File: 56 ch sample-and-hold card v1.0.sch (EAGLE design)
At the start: 116 parts, among them IC1 4051D, IC10 TL074JT, IC11 4051D, IC12 TL074JT, IC13 TL074JT, IC14 4051D, IC15 TL074JT, IC16 TL074JT, IC17 4051D, IC18 TL074JT, IC19 TL074JT, IC20 4051D, IC21 TL074JT, IC22 TL074JT, IC26 4051D, IC27 TL074JT, IC28 TL074JT, IC3 TL074JT, IC5 78L05F, IC6 TL074JT, IC7 4051D, IC9 TL074JT

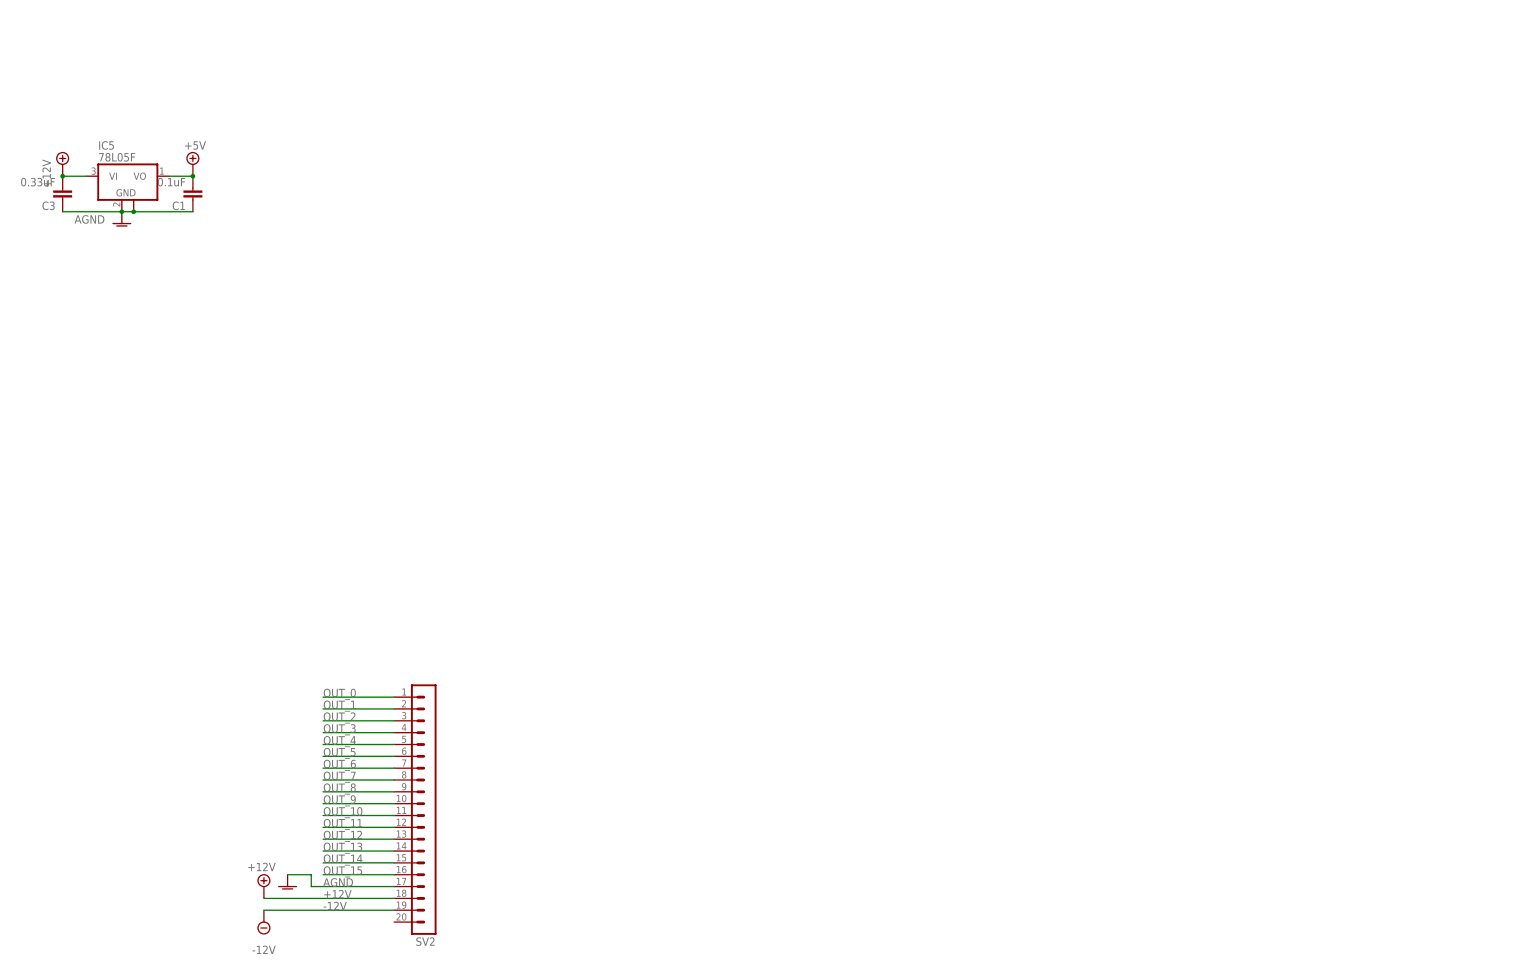
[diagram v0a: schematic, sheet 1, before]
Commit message: All cells for 56ch CV routed
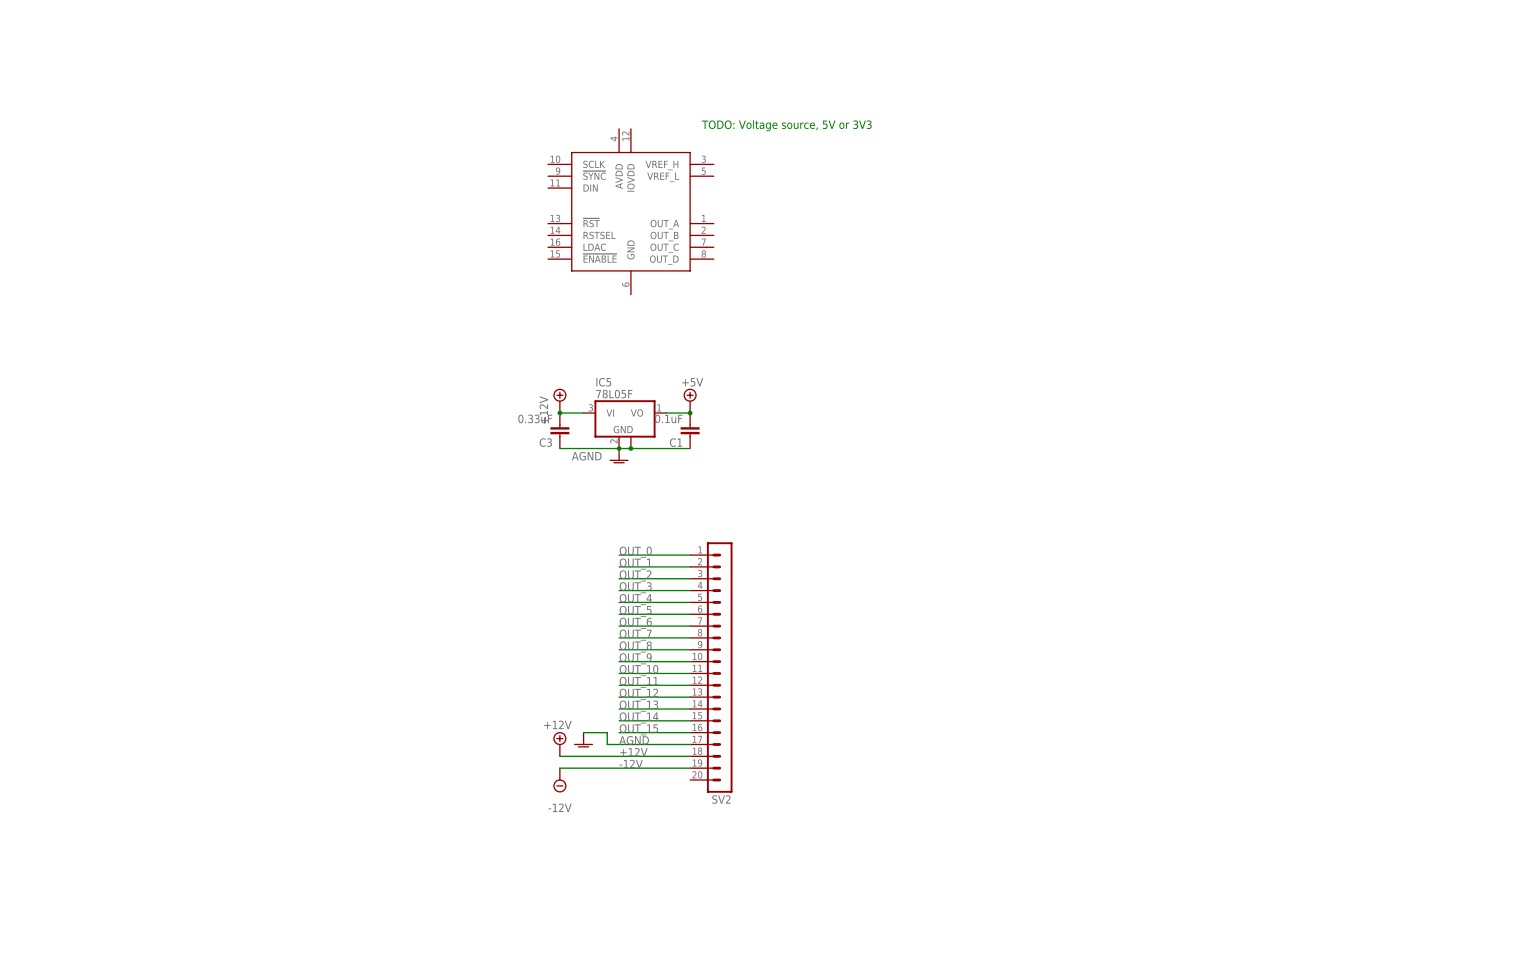
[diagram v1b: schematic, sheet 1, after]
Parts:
- added IC2: DAC8586D, joakim:DAC8586D
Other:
- note added: "TODO: Voltage source, 5V or 3V3"
- moved on the sheet: C1, C3, IC5, SV2

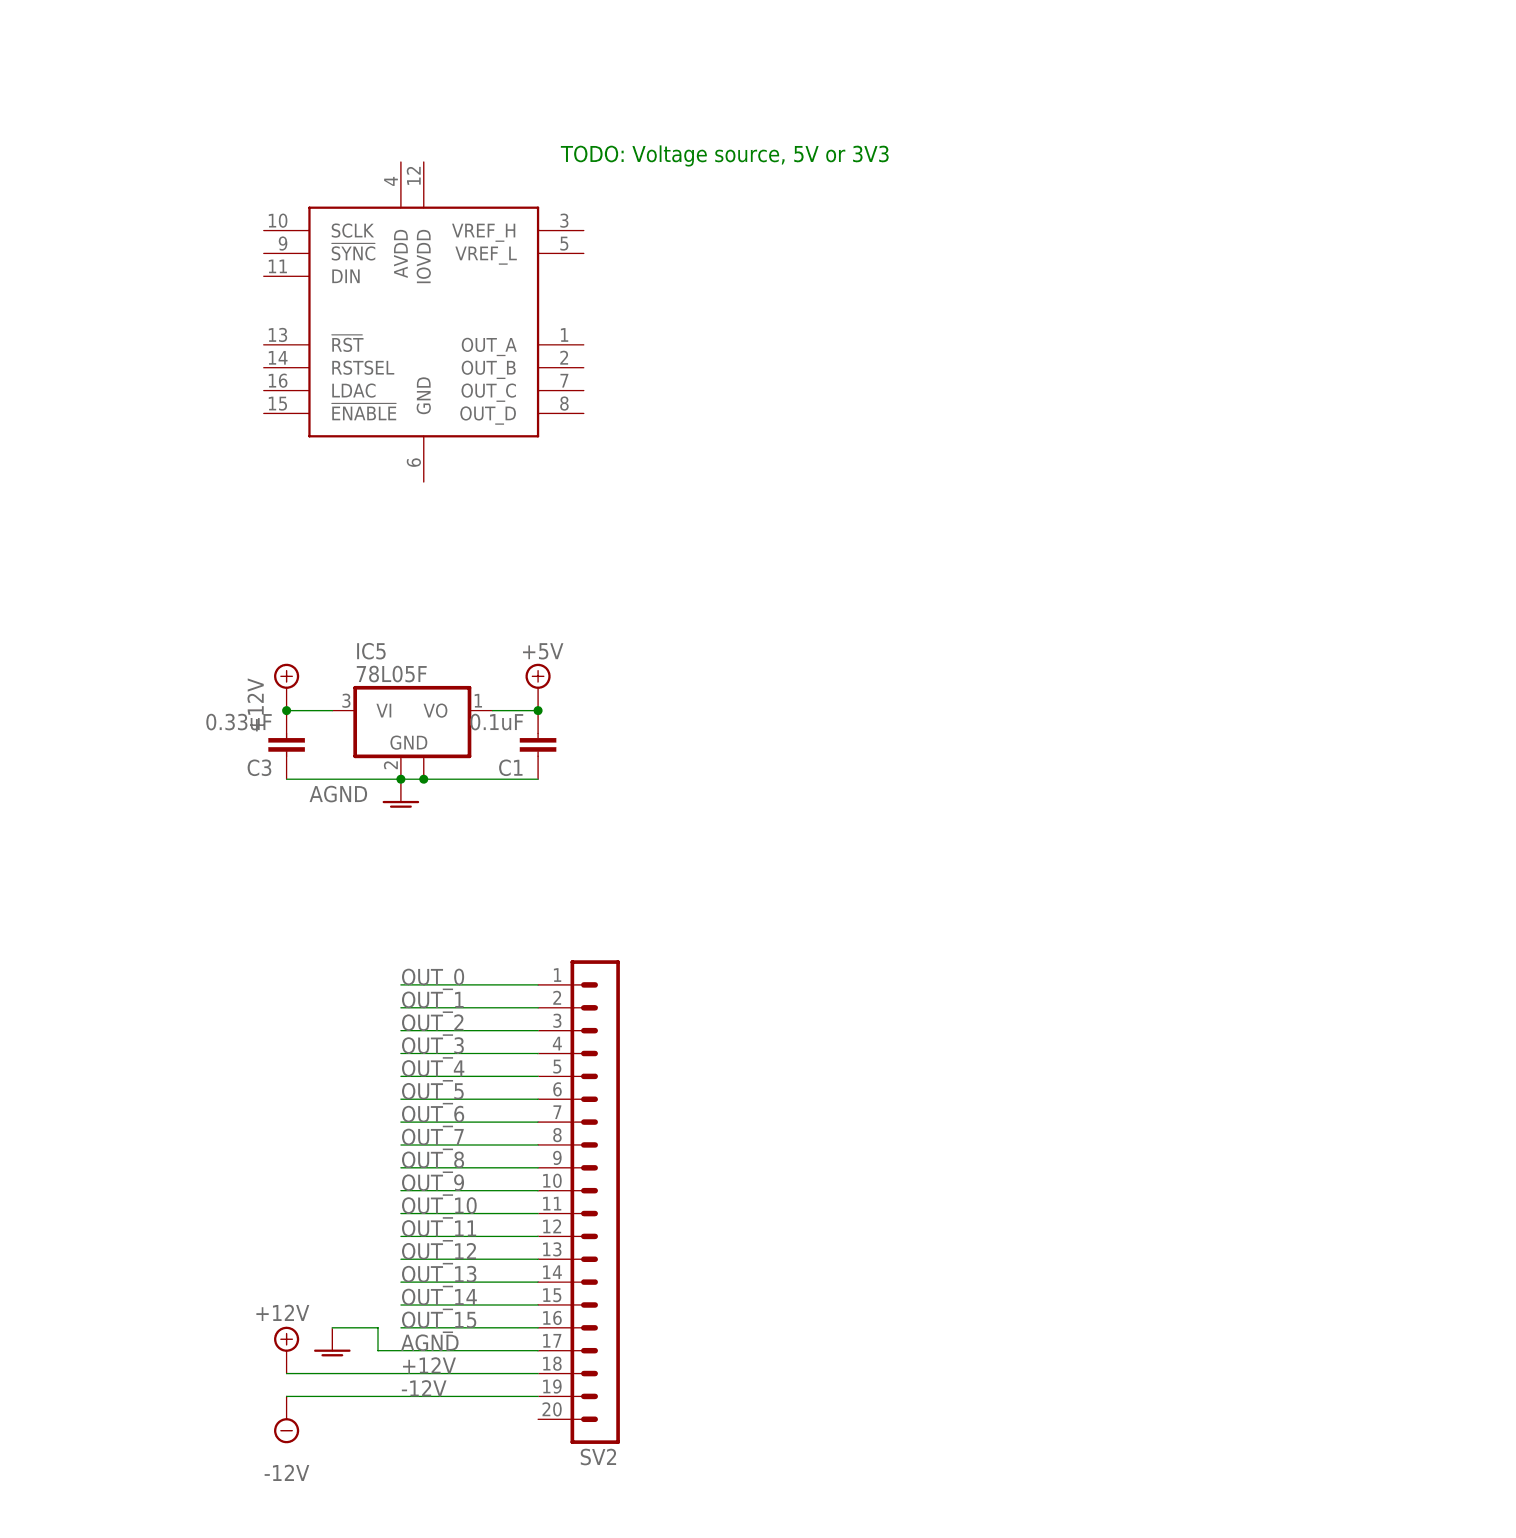
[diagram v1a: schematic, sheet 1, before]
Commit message: Mostly routed, needs DAC testing
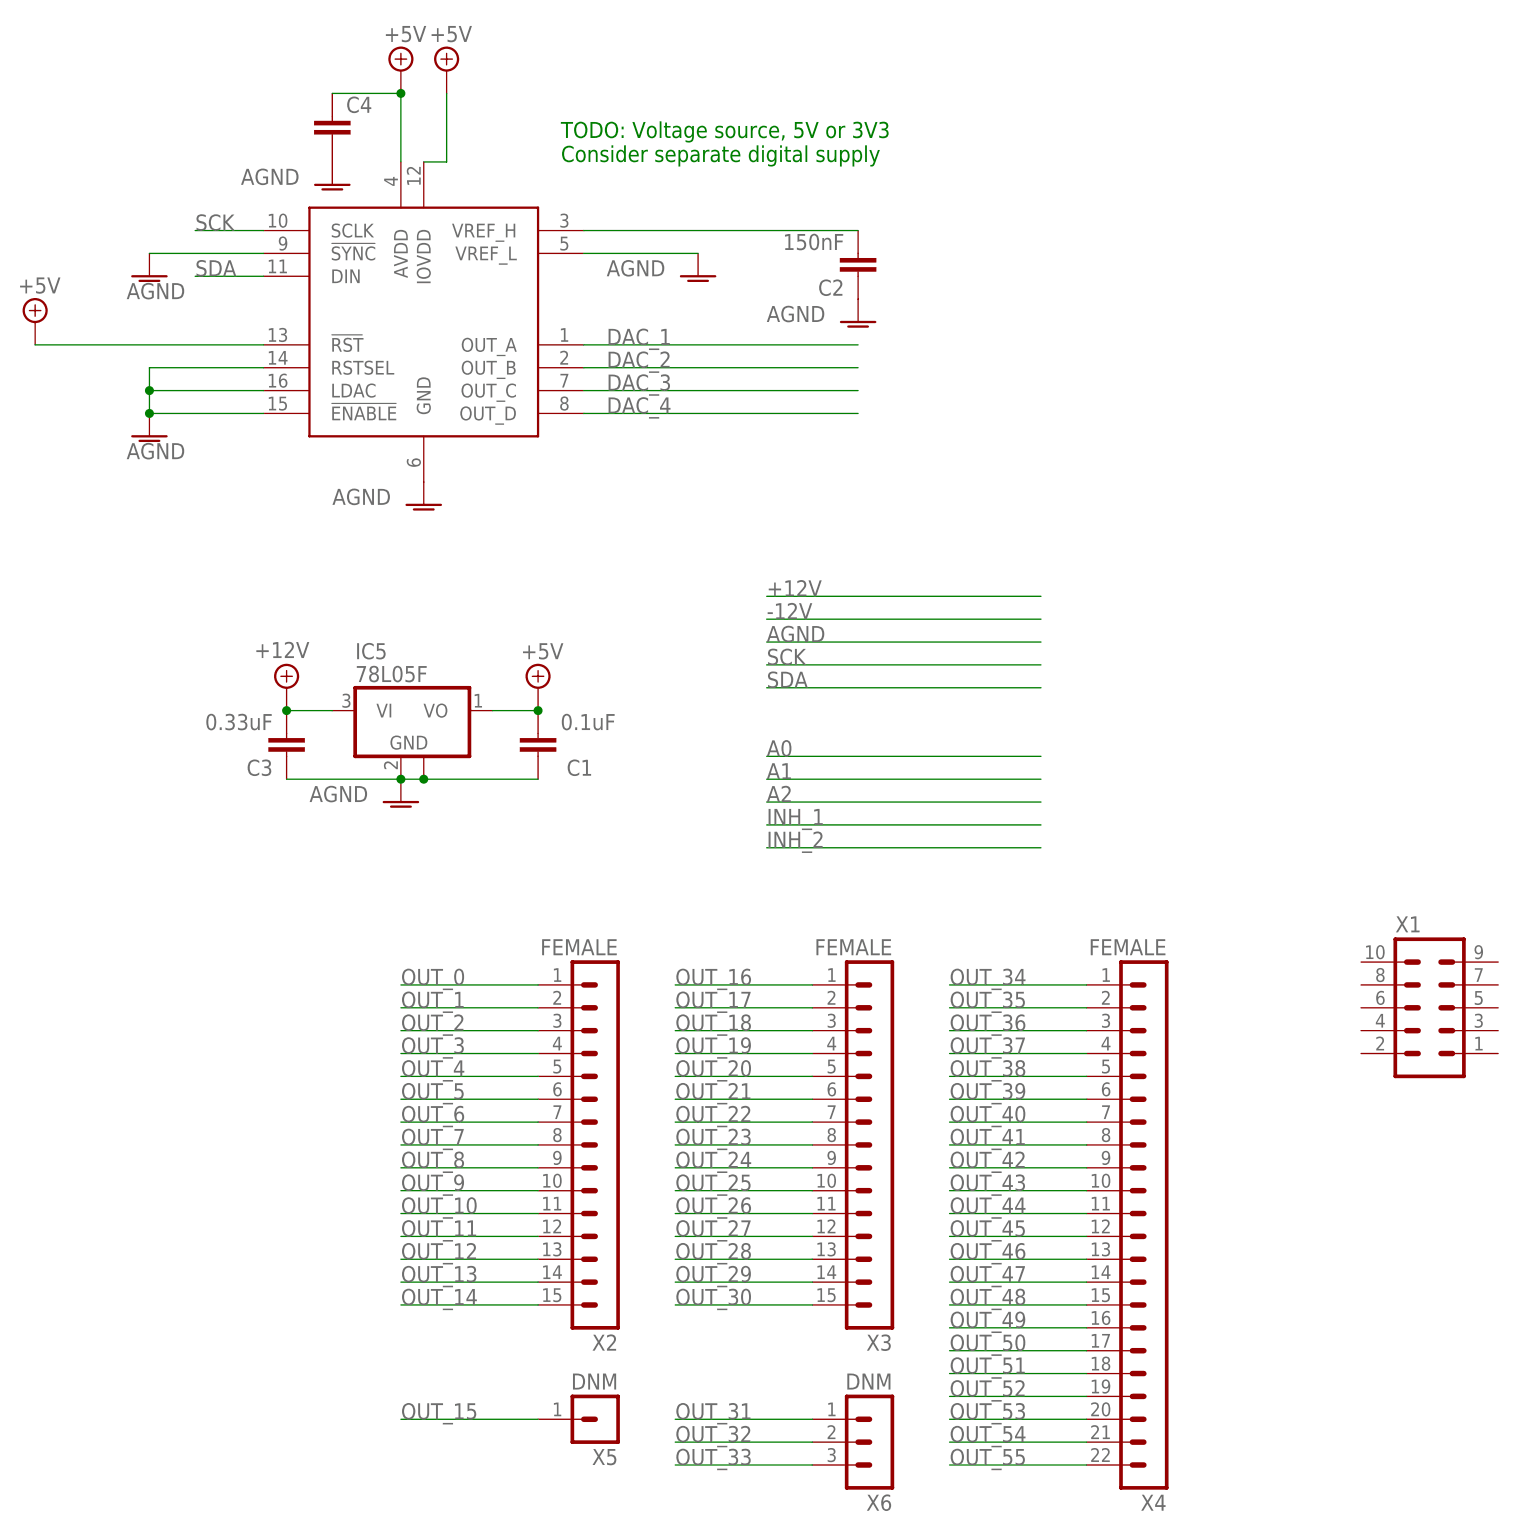
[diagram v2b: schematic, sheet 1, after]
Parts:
- removed SV2: (no value), joakim:MA20-1
- added C2: 150nF, resistor:C-EUC0603
- added C4: (no value), joakim:C-EU-J0402
- added X1: (no value), joakim:MA05-2J
- added X2, X3: FEMALE, joakim:MA15-1JC
- added X4: FEMALE, joakim:MA22-1JC
- added X5: DNM, joakim:MA01-1JN
- added X6: DNM, joakim:MA03-1JN
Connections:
- new net N$8: C2.2, IC2.VREF_H
- new net SCK: IC2.SCLK
- new net SDA: IC2.DIN
- net +12V: no longer SV2.18
- net +5V: now also C4.1, IC2.!RST, IC2.AVDD, IC2.IOVDD
- net -12V: no longer SV2.19
- net AGND: now also C2.1, C4.2, IC2.!ENABLE, IC2.!SYNC, IC2.GND, IC2.LDAC, IC2.RSTSEL, IC2.VREF_L; no longer SV2.17
- net DAC_1: now also IC2.OUT_A, IC26A.X; no longer IC11A.X, IC1A.X
- net DAC_2: now also IC17A.X, IC2.OUT_B, IC20A.X; no longer IC14A.X, IC7A.X
- net DAC_3: now also IC14A.X, IC2.OUT_C, IC7A.X; no longer IC17A.X, IC20A.X
- net DAC_4: now also IC11A.X, IC1A.X, IC2.OUT_D; no longer IC26A.X
- net OUT_0: now also X2.1; no longer SV2.1
- net OUT_1: now also X2.2; no longer SV2.2
- net OUT_10: now also X2.11; no longer SV2.11
- net OUT_11: now also X2.12; no longer SV2.12
- net OUT_12: now also X2.13; no longer SV2.13
- net OUT_13: now also X2.14; no longer SV2.14
- net OUT_14: now also X2.15; no longer SV2.15
- net OUT_15: now also X5.1; no longer SV2.16
- net OUT_16: now also X3.1
- net OUT_17: now also X3.2
- net OUT_18: now also X3.3
- net OUT_19: now also X3.4
- net OUT_2: now also X2.3; no longer SV2.3
- net OUT_20: now also X3.5
- net OUT_21: now also X3.6
- net OUT_22: now also X3.7
- net OUT_23: now also X3.8
- net OUT_24: now also X3.9
- net OUT_25: now also X3.10
- net OUT_26: now also X3.11
- net OUT_27: now also X3.12
- net OUT_28: now also X3.13
- net OUT_29: now also X3.14
- net OUT_3: now also X2.4; no longer SV2.4
- net OUT_30: now also X3.15
- net OUT_31: now also X6.1
- net OUT_32: now also X6.2
- net OUT_33: now also X6.3
- net OUT_34: now also X4.1
- net OUT_35: now also X4.2
- net OUT_36: now also X4.3
- net OUT_37: now also X4.4
- net OUT_38: now also X4.5
- net OUT_39: now also X4.6
- net OUT_4: now also X2.5; no longer SV2.5
- net OUT_40: now also X4.7
- net OUT_41: now also X4.8
- net OUT_42: now also X4.9
- net OUT_43: now also X4.10
- net OUT_44: now also X4.11
- net OUT_45: now also X4.12
- net OUT_46: now also X4.13
- net OUT_47: now also X4.14
- net OUT_48: now also X4.15
- net OUT_49: now also X4.16
- net OUT_5: now also X2.6; no longer SV2.6
- net OUT_50: now also X4.17
- net OUT_51: now also X4.18
- net OUT_52: now also X4.19
- net OUT_53: now also X4.20
- net OUT_54: now also X4.21
- net OUT_55: now also X4.22
- net OUT_6: now also X2.7; no longer SV2.7
- net OUT_7: now also X2.8; no longer SV2.8
- net OUT_8: now also X2.9; no longer SV2.9
- net OUT_9: now also X2.10; no longer SV2.10
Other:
- note added: "TODO: Voltage source, 5V or 3V3 Consider separate digital supply"
- note removed: "TODO: Voltage source, 5V or 3V3"
